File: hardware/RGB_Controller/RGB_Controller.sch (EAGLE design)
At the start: 19 parts, among them IC1 7805TV, J1 J5MM, J2 J5MM, J3 J5MM, Q1 IRF520, Q2 IRF520, Q3 IRF520

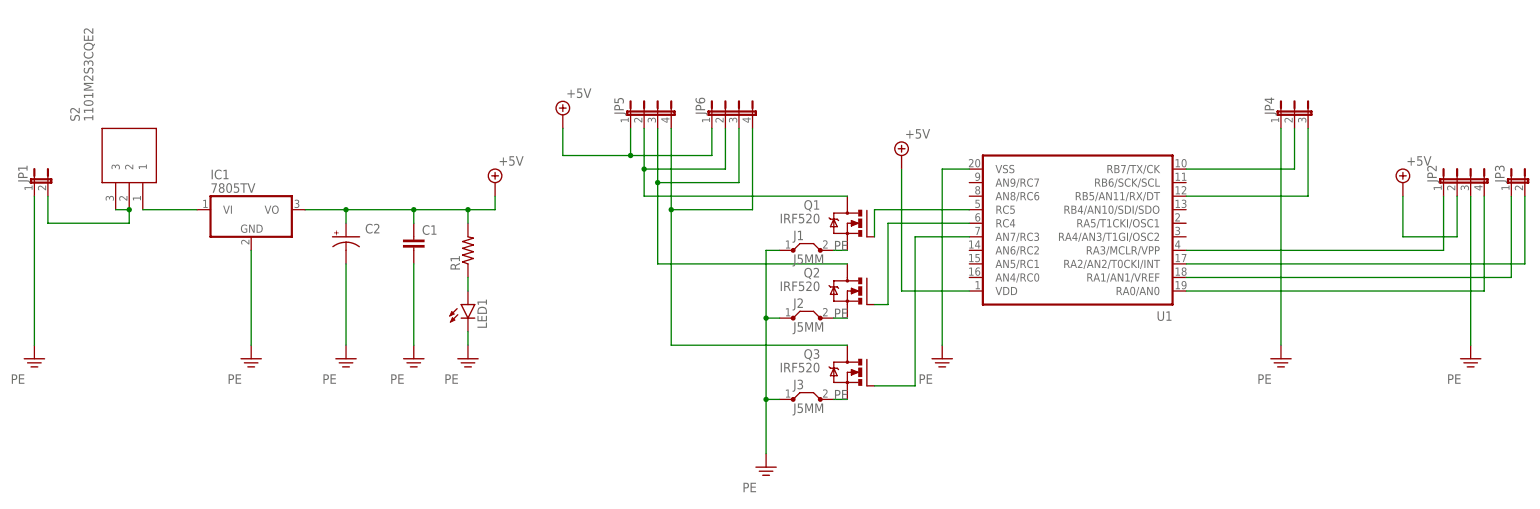
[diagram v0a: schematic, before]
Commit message: Fixed Colour Inconsistency
- Changed flushOutput() from serial to flush() function
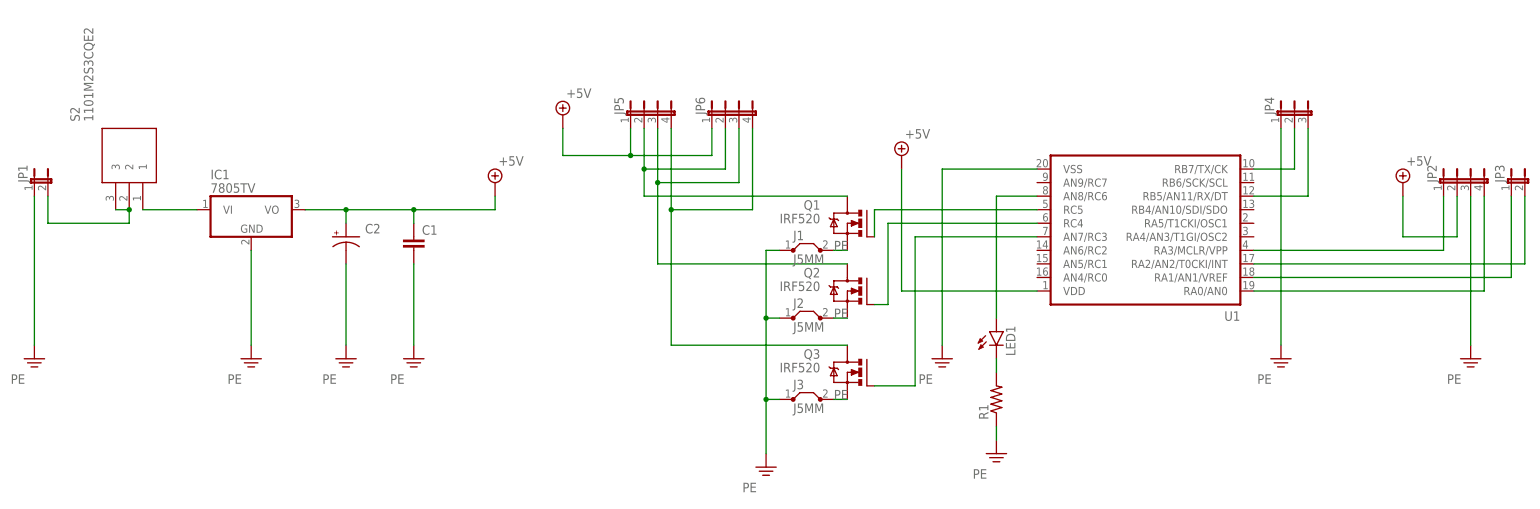
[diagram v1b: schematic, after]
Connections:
- new net N$15: LED1.A, U1.AN8/RC6
- net +5V: no longer R1.2
- net N$3: now also LED1.C, R1.2; no longer LED1.A, R1.1
- net PE: now also R1.1; no longer LED1.C
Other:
- moved on the sheet: LED1, R1, U1
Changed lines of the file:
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@@
 </plain>
 <instances>
-<instance part="R1" gate="G$1" x="43.18" y="78.74" smashed="yes" rot="R90">
-<attribute name="NAME" x="41.6814" y="74.93" size="1.778" layer="95" rot="R90"/>
-<attribute name="VALUE" x="46.482" y="74.93" size="1.778" layer="96" rot="R90"/>
+<instance part="R1" gate="G$1" x="142.24" y="50.8" smashed="yes" rot="R90">
+<attribute name="NAME" x="140.7414" y="46.99" size="1.778" layer="95" rot="R90"/>
+<attribute name="VALUE" x="145.542" y="46.99" size="1.778" layer="96" rot="R90"/>
 </instance>
 <instance part="C1" gate="G$1" x="33.02" y="81.28" smashed="yes">
@@
 <attribute name="VALUE" x="21.336" y="77.089" size="1.778" layer="96"/>
 </instance>
-<instance part="LED1" gate="G$1" x="43.18" y="68.58" smashed="yes">
-<attribute name="NAME" x="46.736" y="64.008" size="1.778" layer="95" rot="R90"/>
-<attribute name="VALUE" x="48.895" y="64.008" size="1.778" layer="96" rot="R90"/>
+<instance part="LED1" gate="G$1" x="142.24" y="63.5" smashed="yes">
+<attribute name="NAME" x="145.796" y="58.928" size="1.778" layer="95" rot="R90"/>
+<attribute name="VALUE" x="147.955" y="58.928" size="1.778" layer="96" rot="R90"/>
 </instance>
 <instance part="IC1" gate="A1" x="2.54" y="86.36" smashed="yes">
@@
 <attribute name="VALUE" x="28.575" y="53.721" size="1.778" layer="96"/>
 </instance>
-<instance part="SUPPLY5" gate="PE" x="43.18" y="58.42" smashed="yes">
-<attribute name="VALUE" x="38.735" y="53.721" size="1.778" layer="96"/>
-</instance>
-<instance part="U1" gate="G$1" x="157.48" y="83.82" smashed="yes" rot="R180">
-<attribute name="NAME" x="175.26" y="67.31" size="1.778" layer="95" rot="R180"/>
-<attribute name="VALUE" x="175.26" y="99.06" size="1.778" layer="96" rot="R180"/>
+<instance part="SUPPLY5" gate="PE" x="142.24" y="40.64" smashed="yes">
+<attribute name="VALUE" x="137.795" y="35.941" size="1.778" layer="96"/>
+</instance>
+<instance part="U1" gate="G$1" x="170.18" y="83.82" smashed="yes" rot="R180">
+<attribute name="NAME" x="187.96" y="67.31" size="1.778" layer="95" rot="R180"/>
+<attribute name="VALUE" x="187.96" y="99.06" size="1.778" layer="96" rot="R180"/>
 </instance>
 <instance part="SUPPLY6" gate="PE" x="132.08" y="58.42" smashed="yes">
@@
 </segment>
 <segment>
-<pinref part="LED1" gate="G$1" pin="C"/>
-<pinref part="SUPPLY5" gate="PE" pin="PE"/>
-<wire x1="43.18" y1="63.5" x2="43.18" y2="60.96" width="0.1524" layer="91"/>
-</segment>
-<segment>
 <pinref part="U1" gate="G$1" pin="VSS"/>
-<wire x1="137.16" y1="93.98" x2="132.08" y2="93.98" width="0.1524" layer="91"/>
+<wire x1="149.86" y1="93.98" x2="132.08" y2="93.98" width="0.1524" layer="91"/>
 <pinref part="SUPPLY6" gate="PE" pin="PE"/>
 <wire x1="132.08" y1="60.96" x2="132.08" y2="93.98" width="0.1524" layer="91"/>
@@
 <label x="111.76" y="50.8" size="1.778" layer="95"/>
 </segment>
-</net>
-<net name="N$3" class="0">
-<segment>
+<segment>
+<pinref part="SUPPLY5" gate="PE" pin="PE"/>
 <pinref part="R1" gate="G$1" pin="1"/>
-<pinref part="LED1" gate="G$1" pin="A"/>
-<wire x1="43.18" y1="73.66" x2="43.18" y2="71.12" width="0.1524" layer="91"/>
+<wire x1="142.24" y1="43.18" x2="142.24" y2="45.72" width="0.1524" layer="91"/>
 </segment>
 </net>
@@
 <wire x1="20.32" y1="83.82" x2="20.32" y2="86.36" width="0.1524" layer="91"/>
 <junction x="20.32" y="86.36"/>
-<pinref part="R1" gate="G$1" pin="2"/>
-<wire x1="43.18" y1="83.82" x2="43.18" y2="86.36" width="0.1524" layer="91"/>
-<wire x1="43.18" y1="86.36" x2="33.02" y2="86.36" width="0.1524" layer="91"/>
-<wire x1="48.26" y1="86.36" x2="43.18" y2="86.36" width="0.1524" layer="91"/>
-<junction x="43.18" y="86.36"/>
+<wire x1="48.26" y1="86.36" x2="33.02" y2="86.36" width="0.1524" layer="91"/>
 <pinref part="SUPPLY1" gate="+5V" pin="+5V"/>
 <wire x1="48.26" y1="88.9" x2="48.26" y2="86.36" width="0.1524" layer="91"/>
@@
 <wire x1="124.46" y1="93.98" x2="124.46" y2="71.12" width="0.1524" layer="91"/>
 <pinref part="U1" gate="G$1" pin="VDD"/>
-<wire x1="124.46" y1="71.12" x2="137.16" y2="71.12" width="0.1524" layer="91"/>
+<wire x1="124.46" y1="71.12" x2="149.86" y2="71.12" width="0.1524" layer="91"/>
 </segment>
 <segment>
@@
 <pinref part="U1" gate="G$1" pin="RA3/MCLR/VPP"/>
 <wire x1="226.06" y1="88.9" x2="226.06" y2="78.74" width="0.1524" layer="91"/>
-<wire x1="226.06" y1="78.74" x2="177.8" y2="78.74" width="0.1524" layer="91"/>
+<wire x1="226.06" y1="78.74" x2="190.5" y2="78.74" width="0.1524" layer="91"/>
 </segment>
 </net>
@@
 <pinref part="U1" gate="G$1" pin="RA0/AN0"/>
 <wire x1="233.68" y1="88.9" x2="233.68" y2="71.12" width="0.1524" layer="91"/>
-<wire x1="233.68" y1="71.12" x2="177.8" y2="71.12" width="0.1524" layer="91"/>
+<wire x1="233.68" y1="71.12" x2="190.5" y2="71.12" width="0.1524" layer="91"/>
 </segment>
 </net>
@@
 <wire x1="238.76" y1="88.9" x2="238.76" y2="73.66" width="0.1524" layer="91"/>
 <pinref part="U1" gate="G$1" pin="RA1/AN1/VREF"/>
-<wire x1="238.76" y1="73.66" x2="177.8" y2="73.66" width="0.1524" layer="91"/>
+<wire x1="238.76" y1="73.66" x2="190.5" y2="73.66" width="0.1524" layer="91"/>
 </segment>
 </net>
@@
 <wire x1="241.3" y1="88.9" x2="241.3" y2="76.2" width="0.1524" layer="91"/>
 <pinref part="U1" gate="G$1" pin="RA2/AN2/T0CKI/INT"/>
-<wire x1="241.3" y1="76.2" x2="177.8" y2="76.2" width="0.1524" layer="91"/>
+<wire x1="241.3" y1="76.2" x2="190.5" y2="76.2" width="0.1524" layer="91"/>
 </segment>
 </net>
@@
 <wire x1="198.12" y1="101.6" x2="198.12" y2="93.98" width="0.1524" layer="91"/>
 <pinref part="U1" gate="G$1" pin="RB7/TX/CK"/>
-<wire x1="198.12" y1="93.98" x2="177.8" y2="93.98" width="0.1524" layer="91"/>
+<wire x1="198.12" y1="93.98" x2="190.5" y2="93.98" width="0.1524" layer="91"/>
 </segment>
 </net>
@@
 <pinref part="U1" gate="G$1" pin="RB5/AN11/RX/DT"/>
 <wire x1="200.66" y1="101.6" x2="200.66" y2="88.9" width="0.1524" layer="91"/>
-<wire x1="200.66" y1="88.9" x2="177.8" y2="88.9" width="0.1524" layer="91"/>
+<wire x1="200.66" y1="88.9" x2="190.5" y2="88.9" width="0.1524" layer="91"/>
 </segment>
 </net>
@@
 <segment>
 <pinref part="U1" gate="G$1" pin="RC5"/>
-<wire x1="137.16" y1="86.36" x2="119.38" y2="86.36" width="0.1524" layer="91"/>
+<wire x1="149.86" y1="86.36" x2="119.38" y2="86.36" width="0.1524" layer="91"/>
 <pinref part="Q1" gate="G$1" pin="G"/>
 <wire x1="119.38" y1="86.36" x2="119.38" y2="81.28" width="0.1524" layer="91"/>
@@
 <segment>
 <pinref part="U1" gate="G$1" pin="RC4"/>
-<wire x1="137.16" y1="83.82" x2="121.92" y2="83.82" width="0.1524" layer="91"/>
+<wire x1="149.86" y1="83.82" x2="121.92" y2="83.82" width="0.1524" layer="91"/>
 <pinref part="Q2" gate="G$1" pin="G"/>
 <wire x1="121.92" y1="83.82" x2="121.92" y2="68.58" width="0.1524" layer="91"/>
@@
 <segment>
 <pinref part="U1" gate="G$1" pin="AN7/RC3"/>
-<wire x1="137.16" y1="81.28" x2="127" y2="81.28" width="0.1524" layer="91"/>
+<wire x1="149.86" y1="81.28" x2="127" y2="81.28" width="0.1524" layer="91"/>
 <wire x1="127" y1="81.28" x2="127" y2="53.34" width="0.1524" layer="91"/>
 <pinref part="Q3" gate="G$1" pin="G"/>
@@
 </segment>
 </net>
+<net name="N$15" class="0">
+<segment>
+<pinref part="U1" gate="G$1" pin="AN8/RC6"/>
+<wire x1="149.86" y1="88.9" x2="142.24" y2="88.9" width="0.1524" layer="91"/>
+<pinref part="LED1" gate="G$1" pin="A"/>
+<wire x1="142.24" y1="66.04" x2="142.24" y2="88.9" width="0.1524" layer="91"/>
+</segment>
+</net>
+<net name="N$3" class="0">
+<segment>
+<pinref part="R1" gate="G$1" pin="2"/>
+<pinref part="LED1" gate="G$1" pin="C"/>
+<wire x1="142.24" y1="55.88" x2="142.24" y2="58.42" width="0.1524" layer="91"/>
+</segment>
+</net>

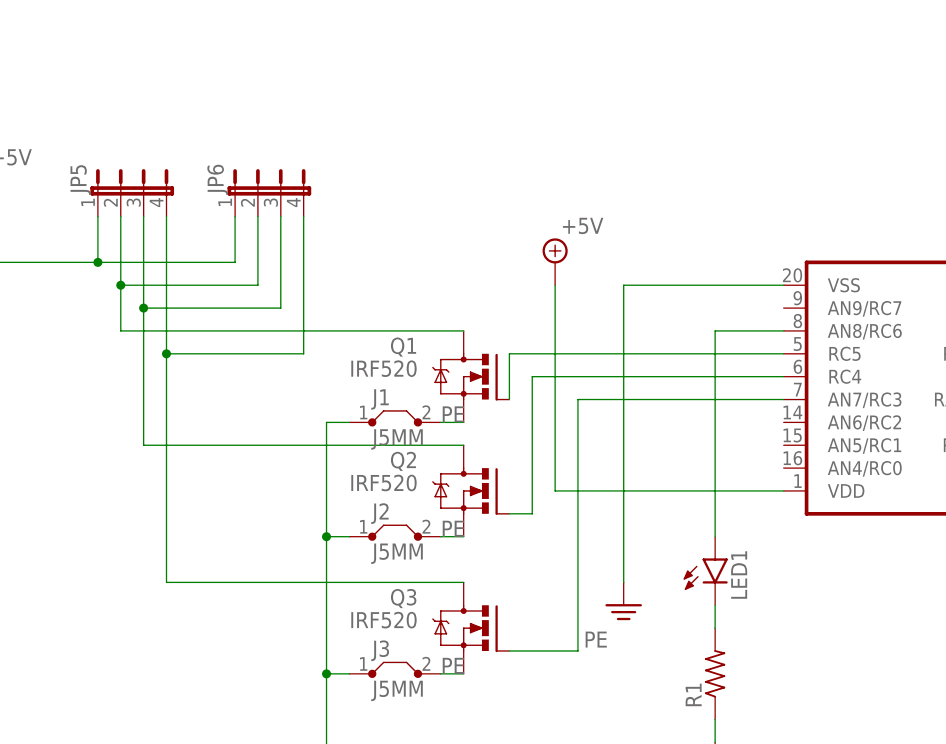
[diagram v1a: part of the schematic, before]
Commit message: Added Sip Pins
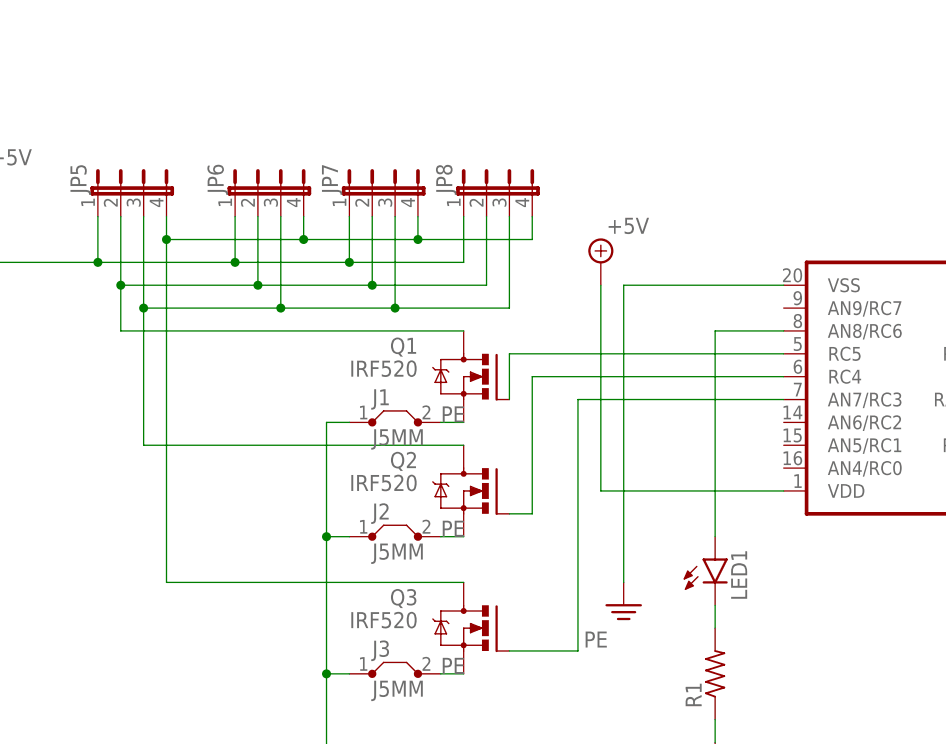
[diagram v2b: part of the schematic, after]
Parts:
- added JP7, JP8: (no value), jumper:JP4E
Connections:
- net +5V: now also JP7.1, JP8.1
- net N$12: now also JP7.2, JP8.2
- net N$13: now also JP7.3, JP8.3
- net N$14: now also JP7.4, JP8.4
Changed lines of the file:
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@@
 <part name="J2" library="jumper" library_urn="urn:adsk.eagle:library:252" deviceset="J" device="5MM" package3d_urn="urn:adsk.eagle:package:15465/1"/>
 <part name="J3" library="jumper" library_urn="urn:adsk.eagle:library:252" deviceset="J" device="5MM" package3d_urn="urn:adsk.eagle:package:15465/1"/>
+<part name="JP7" library="jumper" library_urn="urn:adsk.eagle:library:252" deviceset="JP4E" device="" package3d_urn="urn:adsk.eagle:package:15463/1"/>
+<part name="JP8" library="jumper" library_urn="urn:adsk.eagle:library:252" deviceset="JP4E" device="" package3d_urn="urn:adsk.eagle:package:15463/1"/>
 </parts>
 <sheets>
@@
 <attribute name="VALUE" x="-42.545" y="53.721" size="1.778" layer="96"/>
 </instance>
-<instance part="SUPPLY8" gate="+5V" x="124.46" y="96.52" smashed="yes">
-<attribute name="VALUE" x="125.095" y="99.695" size="1.778" layer="96"/>
+<instance part="SUPPLY8" gate="+5V" x="129.54" y="96.52" smashed="yes">
+<attribute name="VALUE" x="130.175" y="99.695" size="1.778" layer="96"/>
 </instance>
 <instance part="JP2" gate="G$1" x="228.6" y="91.44" smashed="yes">
@@
 <attribute name="NAME" x="104.14" y="52.705" size="1.778" layer="95"/>
 <attribute name="VALUE" x="104.14" y="48.26" size="1.778" layer="96"/>
+</instance>
+<instance part="JP7" gate="G$1" x="104.14" y="104.14" smashed="yes">
+<attribute name="NAME" x="100.33" y="104.14" size="1.778" layer="95" rot="R90"/>
+<attribute name="VALUE" x="112.395" y="104.14" size="1.778" layer="96" rot="R90"/>
+</instance>
+<instance part="JP8" gate="G$1" x="116.84" y="104.14" smashed="yes">
+<attribute name="NAME" x="113.03" y="104.14" size="1.778" layer="95" rot="R90"/>
+<attribute name="VALUE" x="125.095" y="104.14" size="1.778" layer="96" rot="R90"/>
 </instance>
 </instances>
@@
 <segment>
 <pinref part="SUPPLY8" gate="+5V" pin="+5V"/>
-<wire x1="124.46" y1="93.98" x2="124.46" y2="71.12" width="0.1524" layer="91"/>
+<wire x1="129.54" y1="93.98" x2="129.54" y2="71.12" width="0.1524" layer="91"/>
 <pinref part="U1" gate="G$1" pin="VDD"/>
-<wire x1="124.46" y1="71.12" x2="149.86" y2="71.12" width="0.1524" layer="91"/>
+<wire x1="129.54" y1="71.12" x2="149.86" y2="71.12" width="0.1524" layer="91"/>
 </segment>
 <segment>
@@
 <pinref part="JP6" gate="G$1" pin="1"/>
 <wire x1="88.9" y1="96.52" x2="88.9" y2="101.6" width="0.1524" layer="91"/>
+<pinref part="JP7" gate="G$1" pin="1"/>
+<wire x1="101.6" y1="101.6" x2="101.6" y2="96.52" width="0.1524" layer="91"/>
+<wire x1="101.6" y1="96.52" x2="88.9" y2="96.52" width="0.1524" layer="91"/>
+<junction x="88.9" y="96.52"/>
+<pinref part="JP8" gate="G$1" pin="1"/>
+<wire x1="114.3" y1="101.6" x2="114.3" y2="96.52" width="0.1524" layer="91"/>
+<wire x1="114.3" y1="96.52" x2="101.6" y2="96.52" width="0.1524" layer="91"/>
+<junction x="101.6" y="96.52"/>
 </segment>
 </net>
@@
 <pinref part="JP6" gate="G$1" pin="2"/>
 <wire x1="91.44" y1="93.98" x2="91.44" y2="101.6" width="0.1524" layer="91"/>
+<pinref part="JP7" gate="G$1" pin="2"/>
+<wire x1="104.14" y1="101.6" x2="104.14" y2="93.98" width="0.1524" layer="91"/>
+<wire x1="104.14" y1="93.98" x2="91.44" y2="93.98" width="0.1524" layer="91"/>
+<junction x="91.44" y="93.98"/>
+<pinref part="JP8" gate="G$1" pin="2"/>
+<wire x1="116.84" y1="101.6" x2="116.84" y2="93.98" width="0.1524" layer="91"/>
+<wire x1="116.84" y1="93.98" x2="104.14" y2="93.98" width="0.1524" layer="91"/>
+<junction x="104.14" y="93.98"/>
 </segment>
 </net>
@@
 <wire x1="93.98" y1="91.44" x2="78.74" y2="91.44" width="0.1524" layer="91"/>
 <junction x="78.74" y="91.44"/>
+<pinref part="JP7" gate="G$1" pin="3"/>
+<wire x1="106.68" y1="101.6" x2="106.68" y2="91.44" width="0.1524" layer="91"/>
+<wire x1="106.68" y1="91.44" x2="93.98" y2="91.44" width="0.1524" layer="91"/>
+<junction x="93.98" y="91.44"/>
+<pinref part="JP8" gate="G$1" pin="3"/>
+<wire x1="119.38" y1="101.6" x2="119.38" y2="91.44" width="0.1524" layer="91"/>
+<wire x1="119.38" y1="91.44" x2="106.68" y2="91.44" width="0.1524" layer="91"/>
+<junction x="106.68" y="91.44"/>
 </segment>
 </net>
@@
 <segment>
 <pinref part="JP5" gate="G$1" pin="4"/>
-<wire x1="81.28" y1="101.6" x2="81.28" y2="86.36" width="0.1524" layer="91"/>
+<wire x1="81.28" y1="101.6" x2="81.28" y2="99.06" width="0.1524" layer="91"/>
 <pinref part="Q3" gate="G$1" pin="D"/>
-<wire x1="81.28" y1="86.36" x2="81.28" y2="60.96" width="0.1524" layer="91"/>
+<wire x1="81.28" y1="99.06" x2="81.28" y2="60.96" width="0.1524" layer="91"/>
 <wire x1="81.28" y1="60.96" x2="114.3" y2="60.96" width="0.1524" layer="91"/>
 <pinref part="JP6" gate="G$1" pin="4"/>
-<wire x1="96.52" y1="101.6" x2="96.52" y2="86.36" width="0.1524" layer="91"/>
-<wire x1="96.52" y1="86.36" x2="81.28" y2="86.36" width="0.1524" layer="91"/>
-<junction x="81.28" y="86.36"/>
-</segment>
-</net>
+<wire x1="96.52" y1="101.6" x2="96.52" y2="99.06" width="0.1524" layer="91"/>
+<wire x1="96.52" y1="99.06" x2="81.28" y2="99.06" width="0.1524" layer="91"/>
+<junction x="81.28" y="99.06"/>
+<pinref part="JP7" gate="G$1" pin="4"/>
+<wire x1="109.22" y1="101.6" x2="109.22" y2="99.06" width="0.1524" layer="91"/>
+<wire x1="109.22" y1="99.06" x2="96.52" y2="99.06" width="0.1524" layer="91"/>
+<junction x="96.52" y="99.06"/>
+<pinref part="JP8" gate="G$1" pin="4"/>
+<wire x1="121.92" y1="101.6" x2="121.92" y2="99.06" width="0.1524" layer="91"/>
+<wire x1="121.92" y1="99.06" x2="109.22" y2="99.06" width="0.1524" layer="91"/>
+<junction x="109.22" y="99.06"/>
+</segment>
+</net>
